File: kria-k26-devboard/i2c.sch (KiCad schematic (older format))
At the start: 12 parts, among them U12 PCA9306D_118, U13 M24C64-FMC6TG

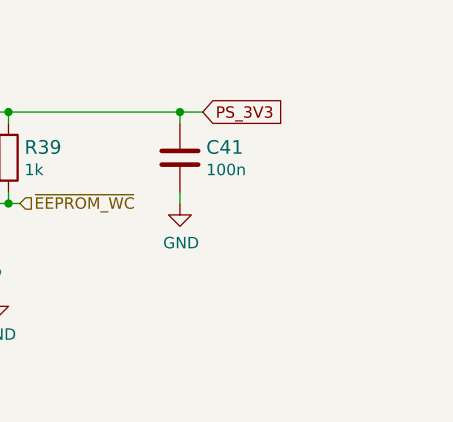
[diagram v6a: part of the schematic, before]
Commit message: Fixes introduced after initial review, length matching double checked with external plugin
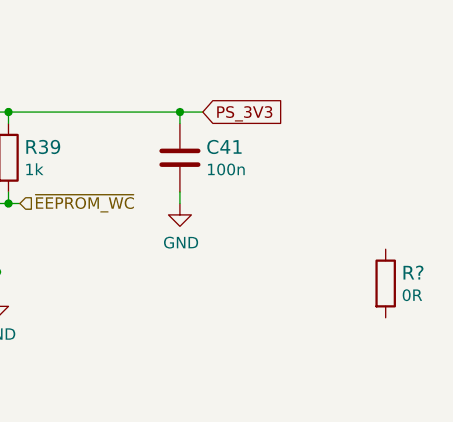
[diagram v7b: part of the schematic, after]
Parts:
- added R?: R_0R_0402, antmicro-footprints:0402-res, symbol antmicroResistors0402:R_0R_0402
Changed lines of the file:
@@
 $Descr A4 11693 8268
 encoding utf-8
-Sheet 7 19
+Sheet 6 19
 Title ""
 Date ""
@@
 Wire Wire Line
 	5050 3700 5400 3700
+$Comp
+L antmicroResistors0402:R_0R_0402 R?
+U 1 1 62876166
+P 10350 3900
+F 0 "R?" V 10305 3970 60  0000 L CNN
+F 1 "R_0R_0402" H 10350 3750 60  0001 C CNN
+F 2 "antmicro-footprints:0402-res" H 10550 4100 60  0001 L CNN
+F 3 "" H 10350 3900 50  0001 C CNN
+F 4 "PANASONIC" H 10550 4300 60  0001 L CNN "Manufacturer"
+F 5 "ERJ2GE0R00X" H 10550 4200 60  0001 L CNN "MPN"
+F 6 "0R" V 10403 3970 50  0000 L CNN "Val"
+F 7 "DNP" V 10350 3900 50  0001 C CNN "DNP"
+	1    10350 3900
+	0    1    1    0
+$EndComp
 $EndSCHEMATC

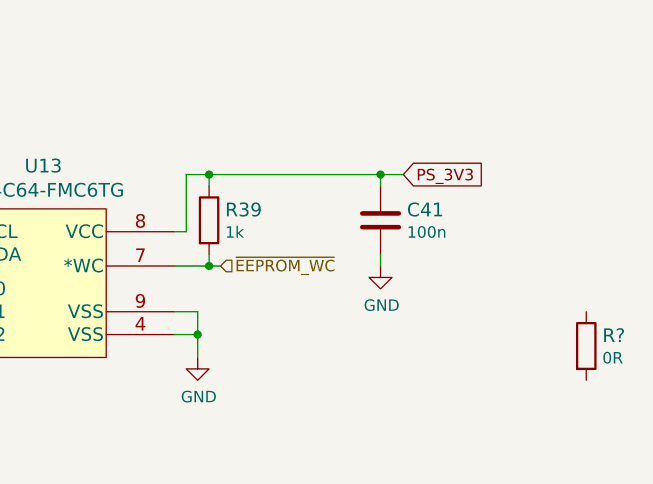
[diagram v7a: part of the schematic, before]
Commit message: Finished implementing changes after the review, fixed ETH led connections, length matching fixed and double checked with external script
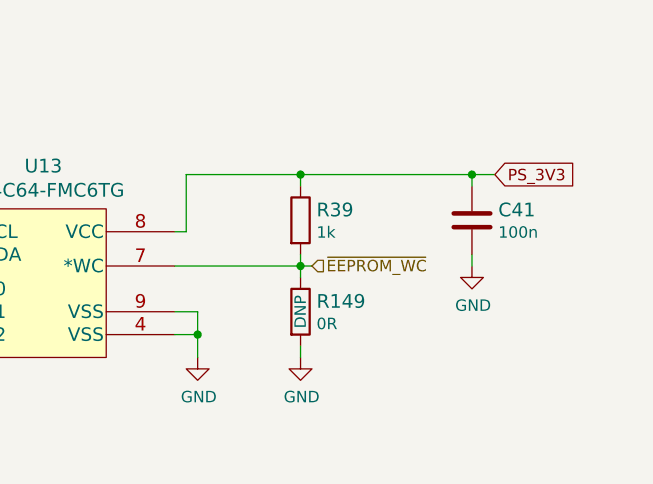
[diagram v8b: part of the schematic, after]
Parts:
- gave numbers to parts that had none: 1
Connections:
- net GND: now also R149.2
- net ~EEPROM_WC: now also R149.1
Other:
- moved on the sheet: C41, R149, R39
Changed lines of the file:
@@
 encoding utf-8
 Sheet 6 19
-Title ""
+Title "I2C"
 Date ""
 Rev ""
@@
 	4750 3800 5050 3800
 Connection ~ 4750 2950
-Text GLabel 9550 3150 2    50   Input ~ 0
+Text GLabel 9950 3150 2    50   Input ~ 0
 PS_3V3
 Wire Wire Line
@@
 	8600 3400 8600 3150
 Wire Wire Line
-	8600 3150 8700 3150
-Wire Wire Line
-	8700 3150 8700 3200
+	8600 3150 9100 3150
+Wire Wire Line
+	9100 3150 9100 3200
 $Comp
 L antmicroCapacitors0402:C_100n_0402 C41
 U 1 1 63AE0E22
-P 9450 3350
-F 0 "C41" H 9335 3305 60  0000 R CNN
-F 1 "C_100n_0402" H 9450 3200 60  0001 C CNN
-F 2 "antmicro-footprints:0402-cap" H 9650 3550 60  0001 L CNN
-F 3 "" H 9450 3350 50  0001 C CNN
-F 4 "Murata" H 9650 3750 60  0001 L CNN "Manufacturer"
-F 5 "GRM155R61H104KE14D" H 9650 3650 60  0001 L CNN "MPN"
-F 6 "100n" H 9335 3403 50  0000 R CNN "Val"
-	1    9450 3350
+P 9850 3350
+F 0 "C41" H 9735 3305 60  0000 R CNN
+F 1 "C_100n_0402" H 9850 3200 60  0001 C CNN
+F 2 "antmicro-footprints:0402-cap" H 10050 3550 60  0001 L CNN
+F 3 "" H 9850 3350 50  0001 C CNN
+F 4 "Murata" H 10050 3750 60  0001 L CNN "Manufacturer"
+F 5 "GRM155R61H104KE14D" H 10050 3650 60  0001 L CNN "MPN"
+F 6 "100n" H 9735 3403 50  0000 R CNN "Val"
+	1    9850 3350
 	-1   0    0    1
 $EndComp
-Connection ~ 8700 3150
-Wire Wire Line
-	9450 3200 9450 3150
+Connection ~ 9100 3150
+Wire Wire Line
+	9850 3200 9850 3150
 $Comp
 L power:GND #PWR067
 U 1 1 63AE2AFC
-P 9450 3550
-F 0 "#PWR067" H 9450 3300 50  0001 C CNN
-F 1 "GND" H 9455 3377 50  0000 C CNN
-F 2 "" H 9450 3550 50  0001 C CNN
-F 3 "" H 9450 3550 50  0001 C CNN
-	1    9450 3550
-	1    0    0    -1
-$EndComp
-Wire Wire Line
-	9450 3550 9450 3500
-Wire Wire Line
-	8700 3550 8700 3500
-Wire Wire Line
-	8550 3550 8700 3550
+P 9850 3550
+F 0 "#PWR067" H 9850 3300 50  0001 C CNN
+F 1 "GND" H 9855 3377 50  0000 C CNN
+F 2 "" H 9850 3550 50  0001 C CNN
+F 3 "" H 9850 3550 50  0001 C CNN
+	1    9850 3550
+	1    0    0    -1
+$EndComp
+Wire Wire Line
+	9850 3550 9850 3500
+Wire Wire Line
+	9100 3550 9100 3500
+Wire Wire Line
+	8550 3550 9100 3550
 $Comp
 L antmicroResistors0402:R_1k_0402 R39
 U 1 1 63ADC97D
-P 8700 3350
-F 0 "R39" V 8655 3420 60  0000 L CNN
-F 1 "R_1k_0402" H 8700 3200 60  0001 C CNN
-F 2 "antmicro-footprints:0402-res" H 8900 3550 60  0001 L CNN
-F 3 "" H 8700 3350 50  0001 C CNN
-F 4 "BOURNS" H 8900 3750 60  0001 L CNN "Manufacturer"
-F 5 "CR0402-FX-1001GLF" H 8900 3650 60  0001 L CNN "MPN"
-F 6 "1k" V 8753 3420 50  0000 L CNN "Val"
-	1    8700 3350
+P 9100 3350
+F 0 "R39" V 9055 3420 60  0000 L CNN
+F 1 "R_1k_0402" H 9100 3200 60  0001 C CNN
+F 2 "antmicro-footprints:0402-res" H 9300 3550 60  0001 L CNN
+F 3 "" H 9100 3350 50  0001 C CNN
+F 4 "BOURNS" H 9300 3750 60  0001 L CNN "Manufacturer"
+F 5 "CR0402-FX-1001GLF" H 9300 3650 60  0001 L CNN "MPN"
+F 6 "1k" V 9153 3420 50  0000 L CNN "Val"
+	1    9100 3350
 	0    1    1    0
 $EndComp
-Connection ~ 9450 3150
-Wire Wire Line
-	9450 3150 9550 3150
-Wire Wire Line
-	8700 3150 9450 3150
-Wire Wire Line
-	8700 3550 8750 3550
-Connection ~ 8700 3550
-Text HLabel 8750 3550 2    50   Input ~ 0
+Connection ~ 9850 3150
+Wire Wire Line
+	9850 3150 9950 3150
+Wire Wire Line
+	9100 3150 9850 3150
+Wire Wire Line
+	9100 3550 9150 3550
+Connection ~ 9100 3550
+Text HLabel 9150 3550 2    50   Input ~ 0
 ~EEPROM_WC
 Text Notes 600  700  0    100  ~ 20
@@
 	5050 3700 5400 3700
 $Comp
-L antmicroResistors0402:R_0R_0402 R?
+L antmicroResistors0402:R_0R_0402 R149
 U 1 1 62876166
-P 10350 3900
-F 0 "R?" V 10305 3970 60  0000 L CNN
-F 1 "R_0R_0402" H 10350 3750 60  0001 C CNN
-F 2 "antmicro-footprints:0402-res" H 10550 4100 60  0001 L CNN
-F 3 "" H 10350 3900 50  0001 C CNN
-F 4 "PANASONIC" H 10550 4300 60  0001 L CNN "Manufacturer"
-F 5 "ERJ2GE0R00X" H 10550 4200 60  0001 L CNN "MPN"
-F 6 "0R" V 10403 3970 50  0000 L CNN "Val"
-F 7 "DNP" V 10350 3900 50  0001 C CNN "DNP"
-	1    10350 3900
+P 9100 3750
+F 0 "R149" V 9055 3820 60  0000 L CNN
+F 1 "R_0R_0402" H 9100 3600 60  0001 C CNN
+F 2 "antmicro-footprints:0402-res" H 9300 3950 60  0001 L CNN
+F 3 "" H 9100 3750 50  0001 C CNN
+F 4 "PANASONIC" H 9300 4150 60  0001 L CNN "Manufacturer"
+F 5 "ERJ2GE0R00X" H 9300 4050 60  0001 L CNN "MPN"
+F 6 "0R" V 9153 3820 50  0000 L CNN "Val"
+F 7 "DNP" H 9100 3750 50  0000 C CNN "DNP"
+	1    9100 3750
 	0    1    1    0
 $EndComp
+Wire Wire Line
+	9100 3600 9100 3550
+$Comp
+L power:GND #PWR0408
+U 1 1 62AEB7B0
+P 9100 3950
+F 0 "#PWR0408" H 9100 3700 50  0001 C CNN
+F 1 "GND" H 9105 3777 50  0000 C CNN
+F 2 "" H 9100 3950 50  0001 C CNN
+F 3 "" H 9100 3950 50  0001 C CNN
+	1    9100 3950
+	1    0    0    -1
+$EndComp
+Wire Wire Line
+	9100 3950 9100 3900
 $EndSCHEMATC
